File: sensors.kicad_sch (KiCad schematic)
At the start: 11 parts, among them U3 LSM6DSOX, U4 LIS2MDL, U7 LPS22DFTR

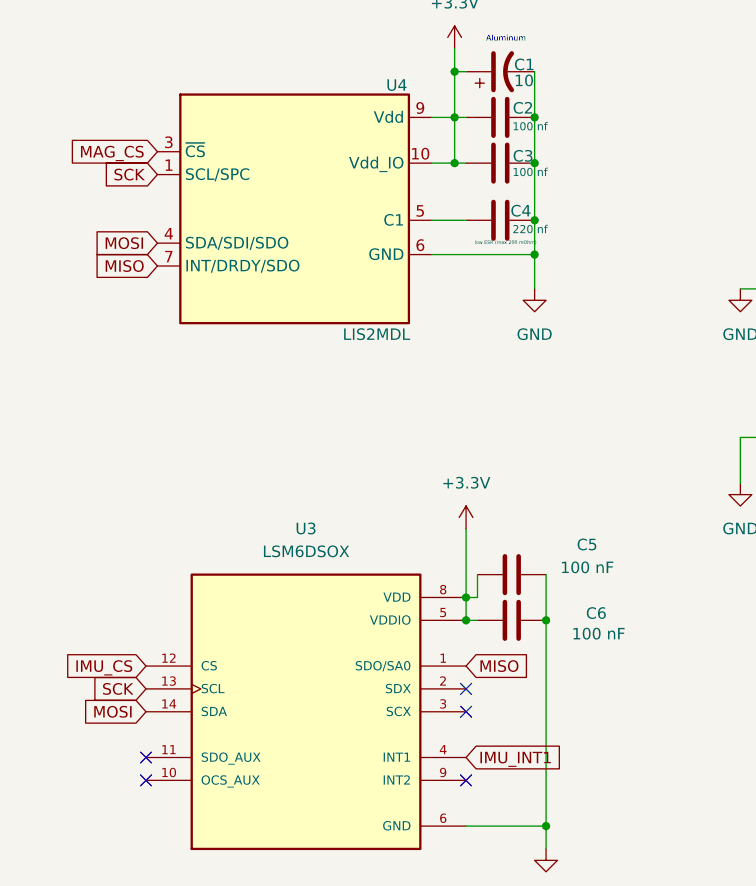
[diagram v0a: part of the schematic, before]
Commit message: Changed the wording of the labels to fit SPI
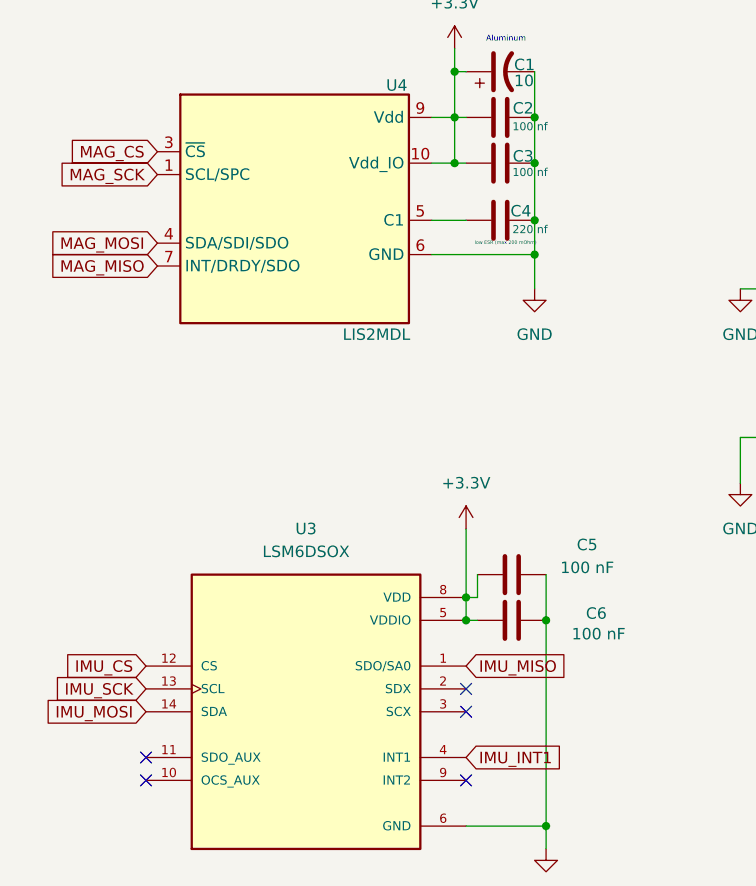
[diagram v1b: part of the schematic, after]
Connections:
- net MISO: no longer U3.1 (SDO/SA0), U4.7 (INT/DRDY/SDO)
- net MOSI: no longer U3.14 (SDA), U4.4 (SDA/SDI/SDO)
- net SCK: no longer U3.13 (SCL), U4.1 (SCL/SPC)
- new net IMU_MISO: U3.1 (SDO/SA0)
- new net IMU_MOSI: U3.14 (SDA)
- new net IMU_SCK: U3.13 (SCL)
- new net MAG_MISO: U4.7 (INT/DRDY/SDO)
- new net MAG_MOSI: U4.4 (SDA/SDI/SDO)
- new net MAG_SCK: U4.1 (SCL/SPC)
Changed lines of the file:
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@@
+		)
+	)
+	(global_label "MAG_MOSI"
+		(shape input)
+		(at 49.53 53.34 180)
+		(fields_autoplaced yes)
+		(effects
+			(font
+				(size 1.27 1.27)
+			)
+			(justify right)
+		)
+		(property "Intersheetrefs" "${INTERSHEET_REFS}"
+			(at 37.171 53.34 0)
+			(effects
+				(font
+					(size 1.27 1.27)
+				)
+				(justify right)
+				(hide yes)
+			)
+		)
+	)
+	(global_label "IMU_INT1"
+		(shape input)
+		(at 83.82 110.49 0)
+		(fields_autoplaced yes)
+		(effects
+			(font
+				(size 1.27 1.27)
+			)
+			(justify left)
+		)
+		(property "Intersheetrefs" "${INTERSHEET_REFS}"
+			(at 95.2719 110.49 0)
+			(effects
+				(font
+					(size 1.27 1.27)
+				)
+				(justify left)
+				(hide yes)
+			)
+		)
+	)
+	(global_label "IMU_MOSI"
+		(shape input)
+		(at 48.26 105.41 180)
+		(fields_autoplaced yes)
+		(effects
+			(font
+				(size 1.27 1.27)
+			)
+			(justify right)
+		)
+		(property "Intersheetrefs" "${INTERSHEET_REFS}"
+			(at 36.3243 105.41 0)
+			(effects
+				(font
+					(size 1.27 1.27)
+				)
+				(justify right)
+				(hide yes)
+			)
+		)
+	)
+	(global_label "BAR_INT"
+		(shape input)
+		(at 198.12 77.47 0)
+		(fields_autoplaced yes)
+		(effects
+			(font
+				(size 1.27 1.27)
+			)
+			(justify left)
+		)
+		(property "Intersheetrefs" "${INTERSHEET_REFS}"
+			(at 208.6043 77.47 0)
+			(effects
+				(font
+					(size 1.27 1.27)
+				)
+				(justify left)
+				(hide yes)
+			)
+		)
+	)
+	(global_label "MAG_MISO"
+		(shape input)
+		(at 49.53 55.88 180)
+		(fields_autoplaced yes)
+		(effects
+			(font
+				(size 1.27 1.27)
+			)
+			(justify right)
+		)
+		(property "Intersheetrefs" "${INTERSHEET_REFS}"
+			(at 37.171 55.88 0)
+			(effects
+				(font
+					(size 1.27 1.27)
+				)
+				(justify right)
+				(hide yes)
+			)
+		)
+	)
+	(global_label "SCK"
+		(shape input)
+		(at 127 72.39 180)
+		(fields_autoplaced yes)
+		(effects
+			(font
+				(size 1.27 1.27)
+			)
+			(justify right)
+		)
+		(property "Intersheetrefs" "${INTERSHEET_REFS}"
+			(at 120.2653 72.39 0)
+			(effects
+				(font
+					(size 1.27 1.27)
+				)
+				(justify right)
+				(hide yes)
+			)
+		)
+	)
+	(global_label "IMU_CS"
+		(shape input)
+		(at 48.26 100.33 180)
+		(fields_autoplaced yes)
+		(effects
+			(font
+				(size 1.27 1.27)
+			)
+			(justify right)
+		)
+		(property "Intersheetrefs" "${INTERSHEET_REFS}"
+			(at 38.441 100.33 0)
+			(effects
+				(font
+					(size 1.27 1.27)
+				)
+				(justify right)
+				(hide yes)
+			)
+		)
+	)
+	(global_label "MAG_SCK"
+		(shape input)
+		(at 49.53 45.72 180)
+		(fields_autoplaced yes)
+		(effects
+			(font
+				(size 1.27 1.27)
+			)
+			(justify right)
+		)
+		(property "Intersheetrefs" "${INTERSHEET_REFS}"
+			(at 38.0177 45.72 0)
+			(effects
+				(font
+					(size 1.27 1.27)
+				)
+				(justify right)
+				(hide yes)
+			)
+		)
+	)
+	(global_label "IMU_MISO"
+		(shape input)
+		(at 83.82 100.33 0)
+		(fields_autoplaced yes)
+		(effects
+			(font
+				(size 1.27 1.27)
+			)
+			(justify left)
+		)
+		(property "Intersheetrefs" "${INTERSHEET_REFS}"
+			(at 95.7557 100.33 0)
+			(effects
+				(font
+					(size 1.27 1.27)
+				)
+				(justify left)
+				(hide yes)
+			)
 		)
 	)
 	(global_label "MOSI"
 		(shape input)
-		(at 49.53 53.34 180)
-		(fields_autoplaced yes)
-		(effects
-			(font
-				(size 1.27 1.27)
-			)
-			(justify right)
-		)
-		(property "Intersheetrefs" "${INTERSHEET_REFS}"
-			(at 41.9486 53.34 0)
-			(effects
-				(font
-					(size 1.27 1.27)
-				)
-				(justify right)
-				(hide yes)
-			)
-		)
-	)
-	(global_label "IMU_INT1"
-		(shape input)
-		(at 83.82 110.49 0)
-		(fields_autoplaced yes)
-		(effects
-			(font
-				(size 1.27 1.27)
-			)
-			(justify left)
-		)
-		(property "Intersheetrefs" "${INTERSHEET_REFS}"
-			(at 95.2719 110.49 0)
-			(effects
-				(font
-					(size 1.27 1.27)
-				)
-				(justify left)
-				(hide yes)
-			)
-		)
-	)
-	(global_label "MOSI"
-		(shape input)
-		(at 48.26 105.41 180)
-		(fields_autoplaced yes)
-		(effects
-			(font
-				(size 1.27 1.27)
-			)
-			(justify right)
-		)
-		(property "Intersheetrefs" "${INTERSHEET_REFS}"
-			(at 40.6786 105.41 0)
-			(effects
-				(font
-					(size 1.27 1.27)
-				)
-				(justify right)
-				(hide yes)
-			)
-		)
-	)
-	(global_label "BAR_INT"
-		(shape input)
-		(at 198.12 77.47 0)
-		(fields_autoplaced yes)
-		(effects
-			(font
-				(size 1.27 1.27)
-			)
-			(justify left)
-		)
-		(property "Intersheetrefs" "${INTERSHEET_REFS}"
-			(at 208.6043 77.47 0)
+		(at 127 77.47 180)
+		(fields_autoplaced yes)
+		(effects
+			(font
+				(size 1.27 1.27)
+			)
+			(justify right)
+		)
+		(property "Intersheetrefs" "${INTERSHEET_REFS}"
+			(at 119.4186 77.47 0)
+			(effects
+				(font
+					(size 1.27 1.27)
+				)
+				(justify right)
+				(hide yes)
+			)
+		)
+	)
+	(global_label "BAR_CS"
+		(shape input)
+		(at 198.12 80.01 0)
+		(fields_autoplaced yes)
+		(effects
+			(font
+				(size 1.27 1.27)
+			)
+			(justify left)
+		)
+		(property "Intersheetrefs" "${INTERSHEET_REFS}"
+			(at 208.1809 80.01 0)
 			(effects
 				(font
@@
 	(global_label "MISO"
 		(shape input)
-		(at 49.53 55.88 180)
-		(fields_autoplaced yes)
-		(effects
-			(font
-				(size 1.27 1.27)
-			)
-			(justify right)
-		)
-		(property "Intersheetrefs" "${INTERSHEET_REFS}"
-			(at 41.9486 55.88 0)
-			(effects
-				(font
-					(size 1.27 1.27)
-				)
-				(justify right)
-				(hide yes)
-			)
-		)
-	)
-	(global_label "SCK"
-		(shape input)
-		(at 127 72.39 180)
-		(fields_autoplaced yes)
-		(effects
-			(font
-				(size 1.27 1.27)
-			)
-			(justify right)
-		)
-		(property "Intersheetrefs" "${INTERSHEET_REFS}"
-			(at 120.2653 72.39 0)
-			(effects
-				(font
-					(size 1.27 1.27)
-				)
-				(justify right)
-				(hide yes)
-			)
-		)
-	)
-	(global_label "IMU_CS"
-		(shape input)
-		(at 48.26 100.33 180)
-		(fields_autoplaced yes)
-		(effects
-			(font
-				(size 1.27 1.27)
-			)
-			(justify right)
-		)
-		(property "Intersheetrefs" "${INTERSHEET_REFS}"
-			(at 38.441 100.33 0)
-			(effects
-				(font
-					(size 1.27 1.27)
-				)
-				(justify right)
-				(hide yes)
-			)
-		)
-	)
-	(global_label "SCK"
-		(shape input)
-		(at 49.53 45.72 180)
-		(fields_autoplaced yes)
-		(effects
-			(font
-				(size 1.27 1.27)
-			)
-			(justify right)
-		)
-		(property "Intersheetrefs" "${INTERSHEET_REFS}"
-			(at 42.7953 45.72 0)
-			(effects
-				(font
-					(size 1.27 1.27)
-				)
-				(justify right)
-				(hide yes)
-			)
-		)
-	)
-	(global_label "MISO"
-		(shape input)
-		(at 83.82 100.33 0)
-		(fields_autoplaced yes)
-		(effects
-			(font
-				(size 1.27 1.27)
-			)
-			(justify left)
-		)
-		(property "Intersheetrefs" "${INTERSHEET_REFS}"
-			(at 91.4014 100.33 0)
-			(effects
-				(font
-					(size 1.27 1.27)
-				)
-				(justify left)
-				(hide yes)
-			)
-		)
-	)
-	(global_label "MOSI"
-		(shape input)
-		(at 127 77.47 180)
-		(fields_autoplaced yes)
-		(effects
-			(font
-				(size 1.27 1.27)
-			)
-			(justify right)
-		)
-		(property "Intersheetrefs" "${INTERSHEET_REFS}"
-			(at 119.4186 77.47 0)
-			(effects
-				(font
-					(size 1.27 1.27)
-				)
-				(justify right)
-				(hide yes)
-			)
-		)
-	)
-	(global_label "BAR_CS"
-		(shape input)
-		(at 198.12 80.01 0)
-		(fields_autoplaced yes)
-		(effects
-			(font
-				(size 1.27 1.27)
-			)
-			(justify left)
-		)
-		(property "Intersheetrefs" "${INTERSHEET_REFS}"
-			(at 208.1809 80.01 0)
-			(effects
-				(font
-					(size 1.27 1.27)
-				)
-				(justify left)
-				(hide yes)
-			)
-		)
-	)
-	(global_label "MISO"
-		(shape input)
 		(at 127 80.01 180)
 		(fields_autoplaced yes)
@@
 		)
 	)
-	(global_label "SCK"
+	(global_label "IMU_SCK"
 		(shape input)
 		(at 48.26 102.87 180)
@@
 		)
 		(property "Intersheetrefs" "${INTERSHEET_REFS}"
-			(at 41.5253 102.87 0)
-			(effects
-				(font
+			(at 37.171 102.87 0)
+			(effects
+				(font

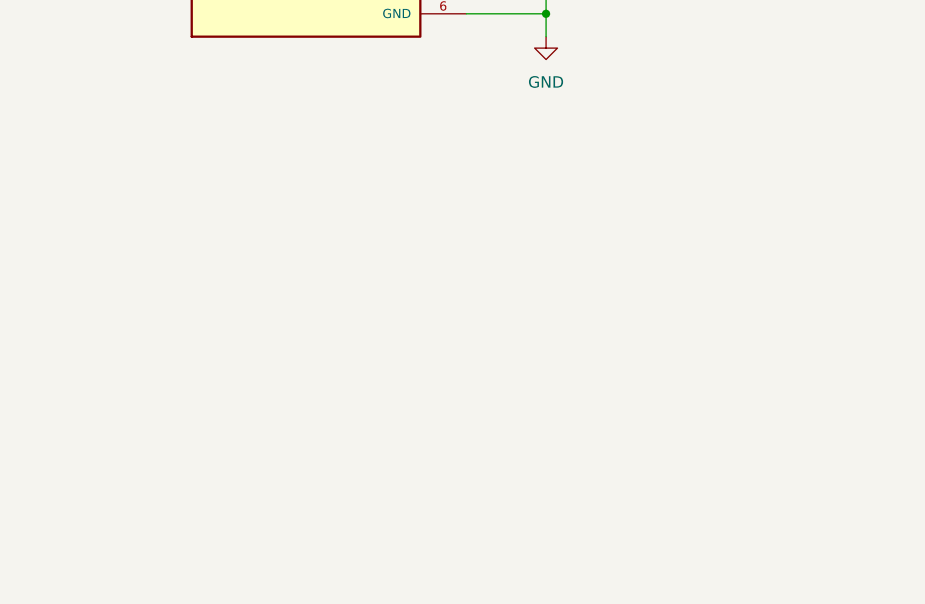
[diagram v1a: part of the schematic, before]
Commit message: Moved the GPS to the sensors sheet and removed the GPS sheet.
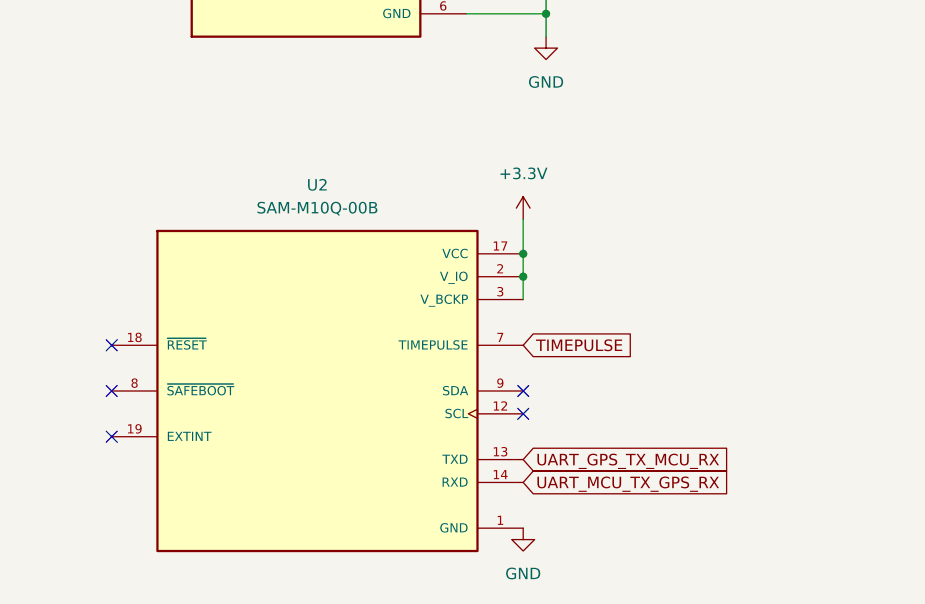
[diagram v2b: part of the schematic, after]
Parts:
- added U2: SAM-M10Q-00B, symbol GP_GPS:SAM-M10Q-00B
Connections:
- net +3.3V: now also U2.17 (VCC), U2.2 (V_IO), U2.3 (V_BCKP)
- net GND: now also U2.1 (GND), U2.10 (GND), U2.11 (GND), U2.15 (GND), U2.16 (GND), U2.20 (GND), U2.4 (GND), U2.5 (GND), U2.6 (GND)
- new net TIMEPULSE: U2.7 (TIMEPULSE)
- new net UART_GPS_TX_MCU_RX: U2.13 (TXD)
- new net UART_MCU_TX_GPS_RX: U2.14 (RXD)
- no-connect marks 5 -> 10

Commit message: Changed the Capacitors to 0603_1608
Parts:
- C1, C10, C2, C3, C4, C5, C6, C9: footprint Capacitor_SMD:C_0201_0603Metric -> Capacitor_SMD:C_0603_1608Metric
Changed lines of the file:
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@@
 			)
 		)
-		(property "Footprint" "Capacitor_SMD:C_0201_0603Metric"
+		(property "Footprint" "Capacitor_SMD:C_0603_1608Metric"
 			(at 92.71 89.2048 0)
 			(effects
@@
 			)
 		)
-		(property "Footprint" "Capacitor_SMD:C_0201_0603Metric"
+		(property "Footprint" "Capacitor_SMD:C_0603_1608Metric"
 			(at 92.71 94.2848 0)
 			(effects
@@
 			)
 		)
-		(property "Footprint" "Capacitor_SMD:C_0201_0603Metric"
+		(property "Footprint" "Capacitor_SMD:C_0603_1608Metric"
 			(at 215.9 63.8048 0)
 			(effects
@@
 			)
 		)
-		(property "Footprint" "Capacitor_SMD:C_0201_0603Metric"
+		(property "Footprint" "Capacitor_SMD:C_0603_1608Metric"
 			(at 91.44 38.4048 0)
 			(effects
@@
 			)
 		)
-		(property "Footprint" "Capacitor_SMD:C_0201_0603Metric"
+		(property "Footprint" "Capacitor_SMD:C_0603_1608Metric"
 			(at 134.62 57.4548 0)
 			(effects
@@
 			)
 		)
-		(property "Footprint" "Capacitor_SMD:C_0201_0603Metric"
+		(property "Footprint" "Capacitor_SMD:C_0603_1608Metric"
 			(at 87.63 34.29 0)
 			(effects
@@
 			)
 		)
-		(property "Footprint" "Capacitor_SMD:C_0201_0603Metric"
+		(property "Footprint" "Capacitor_SMD:C_0603_1608Metric"
 			(at 91.44 49.8348 0)
 			(effects
@@
 			)
 		)
-		(property "Footprint" "Capacitor_SMD:C_0201_0603Metric"
+		(property "Footprint" "Capacitor_SMD:C_0603_1608Metric"
 			(at 91.44 43.4848 0)
 			(effects
